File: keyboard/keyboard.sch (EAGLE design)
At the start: 47 parts, among them SW1 CHERRY_MX, SW10 CHERRY_MX, SW11 CHERRY_MX, SW12 CHERRY_MX, SW13 CHERRY_MX, SW14 CHERRY_MX, SW15 CHERRY_MX, SW16 CHERRY_MX, SW17 CHERRY_MX, SW18 CHERRY_MX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

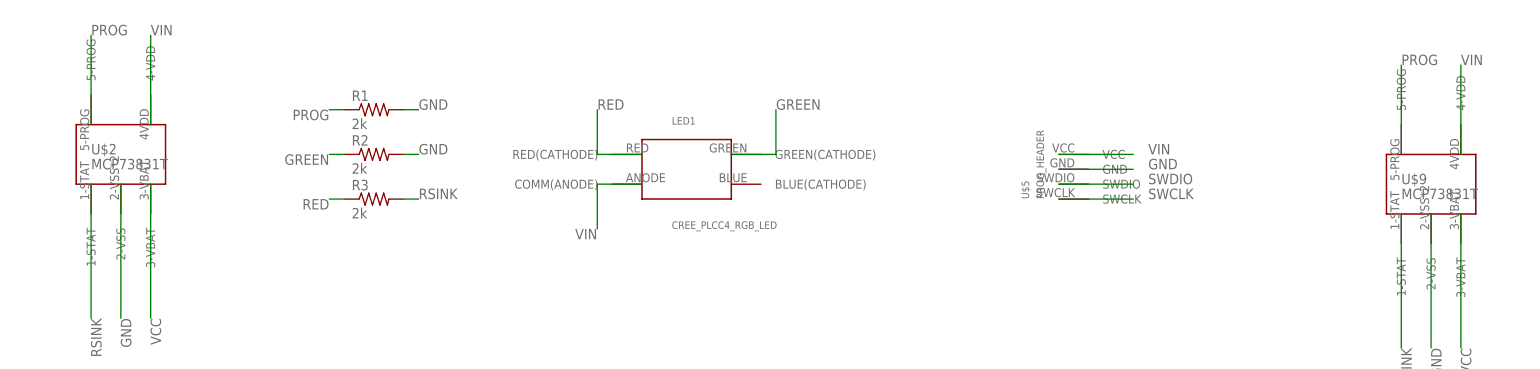
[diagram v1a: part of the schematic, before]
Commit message: redesign heatsink
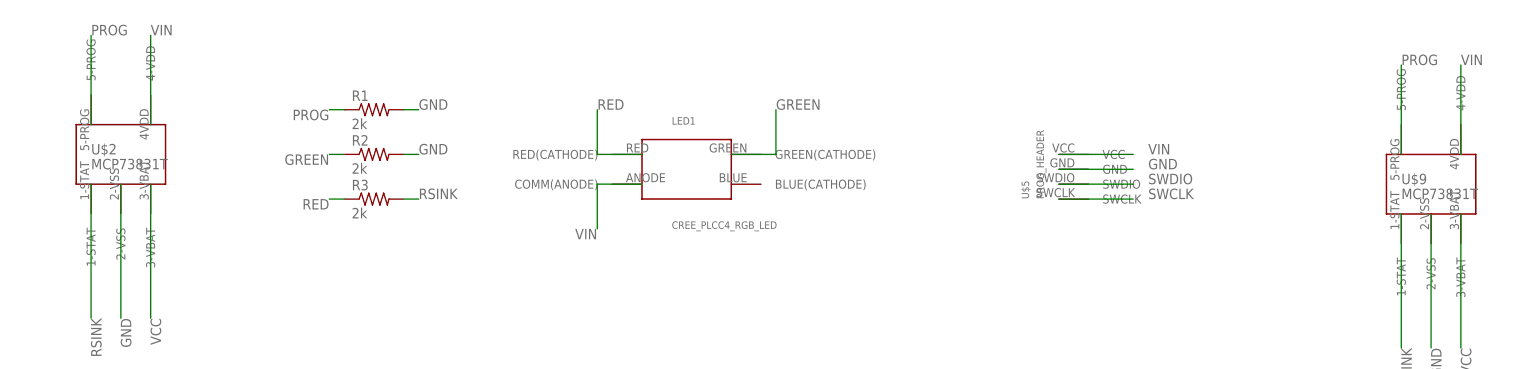
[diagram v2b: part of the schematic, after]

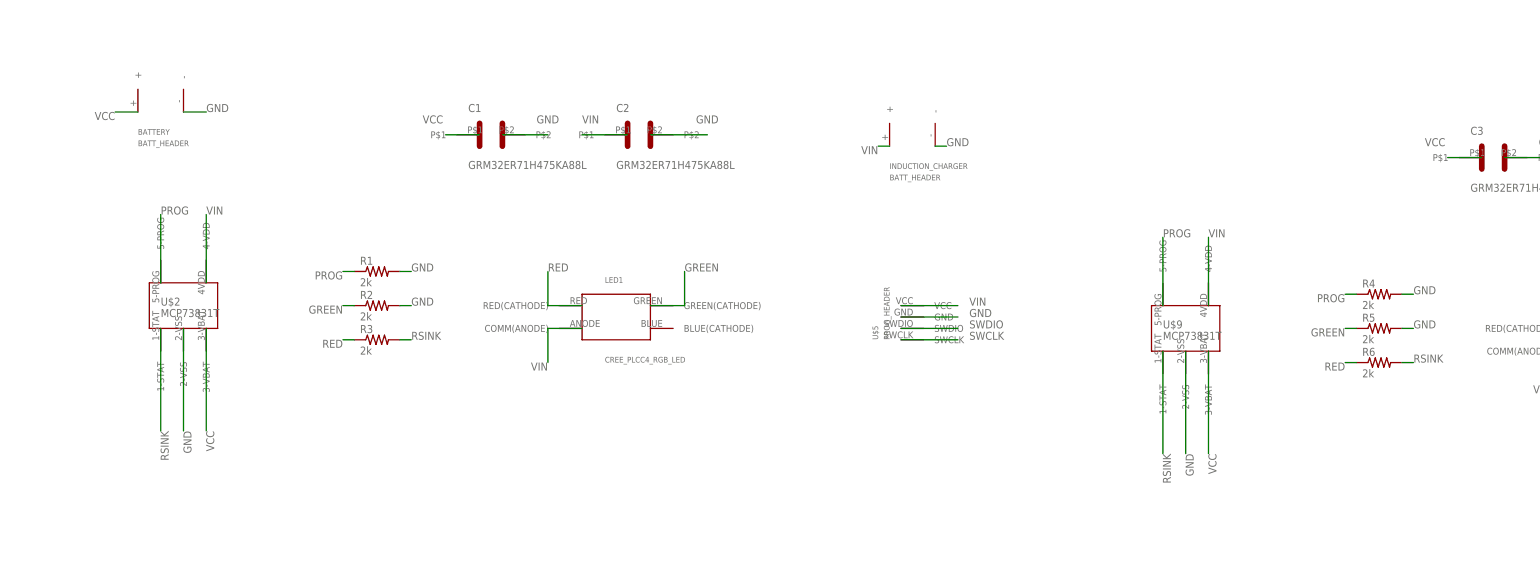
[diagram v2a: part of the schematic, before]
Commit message: add voltage regulator
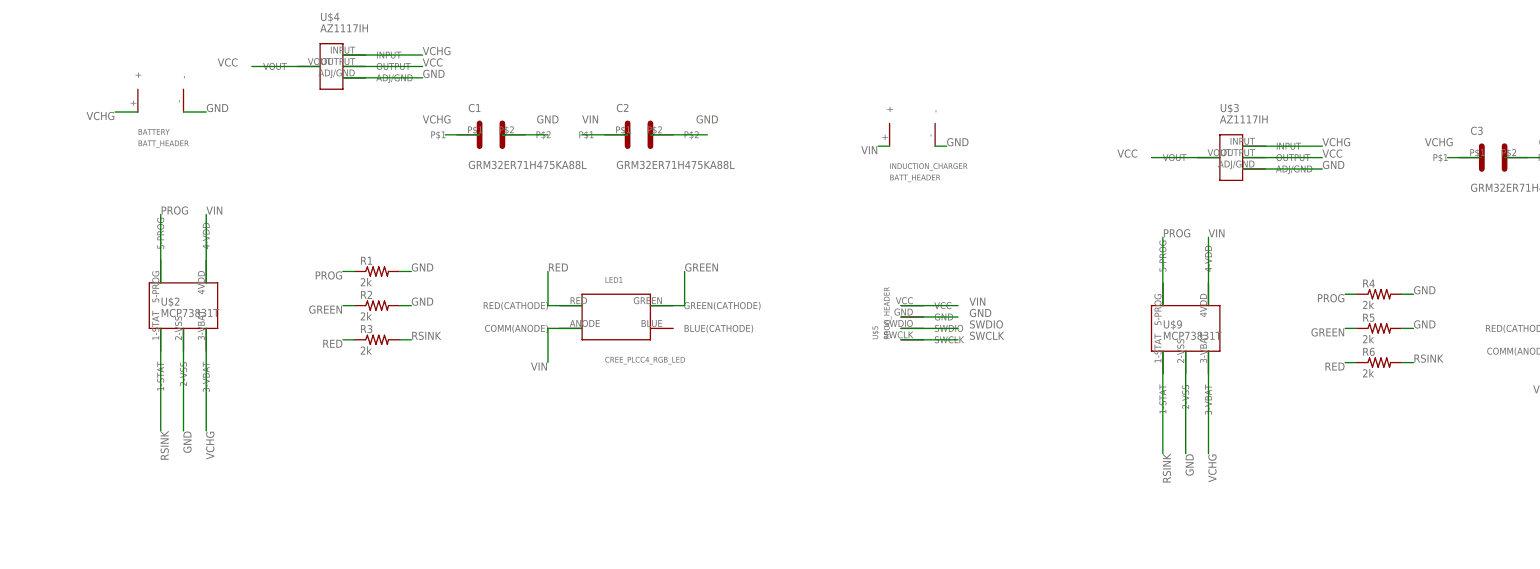
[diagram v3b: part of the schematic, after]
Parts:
- added U$3, U$4: AZ1117IH, az1117ih:AZ1117IH
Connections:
- new net VCHG: BATTERY.+, C1.P$1, C3.P$1, U$2.3-VBAT, U$3.INPUT, U$4.INPUT, U$9.3-VBAT
- net GND: now also U$3.ADJ/GND, U$4.ADJ/GND
- net VCC: now also U$3.OUTPUT, U$3.VOUT, U$4.OUTPUT, U$4.VOUT; no longer BATTERY.+, C1.P$1, C3.P$1, U$2.3-VBAT, U$9.3-VBAT
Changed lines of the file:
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@@
 <?xml version="1.0" encoding="utf-8"?>
 <!DOCTYPE eagle SYSTEM "eagle.dtd">
-<eagle version="8.5.0">
+<eagle version="8.5.2">
 <drawing>
 <settings>
@@
 <part name="INDUCTION_CHARGER" library="batt_header" deviceset="BATT_HEADER" device=""/>
 <part name="BATTERY" library="batt_header" deviceset="BATT_HEADER" device=""/>
+<part name="U$3" library="az1117ih" deviceset="AZ1117IH" device=""/>
+<part name="U$4" library="az1117ih" deviceset="AZ1117IH" device=""/>
 </parts>
 <sheets>
@@
 <instance part="INDUCTION_CHARGER" gate="G$1" x="208.28" y="68.58"/>
 <instance part="BATTERY" gate="G$1" x="40.64" y="76.2"/>
+<instance part="U$3" gate="G$1" x="279.4" y="66.04"/>
+<instance part="U$4" gate="G$1" x="78.74" y="86.36"/>
 </instances>
 <busses>
@@
 <label x="50.8" y="76.2" size="1.778" layer="95"/>
 </segment>
+<segment>
+<pinref part="U$3" gate="G$1" pin="ADJ/GND"/>
+<wire x1="281.94" y1="63.5" x2="299.72" y2="63.5" width="0.1524" layer="91"/>
+<label x="299.72" y="63.5" size="1.778" layer="95"/>
+</segment>
+<segment>
+<pinref part="U$4" gate="G$1" pin="ADJ/GND"/>
+<wire x1="81.28" y1="83.82" x2="99.06" y2="83.82" width="0.1524" layer="91"/>
+<label x="99.06" y="83.82" size="1.778" layer="95"/>
+</segment>
 </net>
 <net name="SW1" class="0">
@@
 </segment>
 <segment>
-<pinref part="U$2" gate="G$1" pin="3-VBAT"/>
-<wire x1="50.8" y1="27.94" x2="50.8" y2="5.08" width="0.1524" layer="91"/>
-<label x="50.8" y="5.08" size="1.778" layer="95" rot="R270"/>
-</segment>
-<segment>
 <pinref part="U$6" gate="G$1" pin="VCC"/>
 <wire x1="236.22" y1="-276.86" x2="218.44" y2="-276.86" width="0.1524" layer="91"/>
@@
 </segment>
 <segment>
-<pinref part="C1" gate="G$1" pin="P$1"/>
-<wire x1="111.76" y1="71.12" x2="104.14" y2="71.12" width="0.1524" layer="91"/>
-<label x="99.06" y="73.66" size="1.778" layer="95"/>
-</segment>
-<segment>
-<pinref part="U$9" gate="G$1" pin="3-VBAT"/>
-<wire x1="274.32" y1="22.86" x2="274.32" y2="0" width="0.1524" layer="91"/>
-<label x="274.32" y="0" size="1.778" layer="95" rot="R270"/>
-</segment>
-<segment>
-<pinref part="C3" gate="G$1" pin="P$1"/>
-<wire x1="335.28" y1="66.04" x2="327.66" y2="66.04" width="0.1524" layer="91"/>
-<label x="322.58" y="68.58" size="1.778" layer="95"/>
-</segment>
-<segment>
-<pinref part="BATTERY" gate="G$1" pin="+"/>
-<wire x1="35.56" y1="76.2" x2="30.48" y2="76.2" width="0.1524" layer="91"/>
-<label x="30.48" y="76.2" size="1.778" layer="95" rot="R180"/>
+<pinref part="U$3" gate="G$1" pin="VOUT"/>
+<wire x1="276.86" y1="66.04" x2="261.62" y2="66.04" width="0.1524" layer="91"/>
+<label x="254" y="66.04" size="1.778" layer="95"/>
+</segment>
+<segment>
+<pinref part="U$3" gate="G$1" pin="OUTPUT"/>
+<wire x1="281.94" y1="66.04" x2="299.72" y2="66.04" width="0.1524" layer="91"/>
+<label x="299.72" y="66.04" size="1.778" layer="95"/>
+</segment>
+<segment>
+<pinref part="U$4" gate="G$1" pin="VOUT"/>
+<wire x1="76.2" y1="86.36" x2="60.96" y2="86.36" width="0.1524" layer="91"/>
+<label x="53.34" y="86.36" size="1.778" layer="95"/>
+</segment>
+<segment>
+<pinref part="U$4" gate="G$1" pin="OUTPUT"/>
+<wire x1="81.28" y1="86.36" x2="99.06" y2="86.36" width="0.1524" layer="91"/>
+<label x="99.06" y="86.36" size="1.778" layer="95"/>
 </segment>
 </net>
@@
 </segment>
 <segment>
+<pinref part="INDUCTION_CHARGER" gate="G$1" pin="+"/>
+<wire x1="203.2" y1="68.58" x2="200.66" y2="68.58" width="0.1524" layer="91"/>
+<label x="200.66" y="68.58" size="1.778" layer="95" rot="R180"/>
+</segment>
+<segment>
 <pinref part="C4" gate="G$1" pin="P$1"/>
 <wire x1="368.3" y1="66.04" x2="358.14" y2="66.04" width="0.1524" layer="91"/>
 <label x="358.14" y="68.58" size="1.778" layer="95"/>
 </segment>
-<segment>
-<pinref part="INDUCTION_CHARGER" gate="G$1" pin="+"/>
-<wire x1="203.2" y1="68.58" x2="200.66" y2="68.58" width="0.1524" layer="91"/>
-<label x="200.66" y="68.58" size="1.778" layer="95" rot="R180"/>
-</segment>
 </net>
 <net name="PROG" class="0">
@@
 </segment>
 </net>
+<net name="VCHG" class="0">
+<segment>
+<pinref part="U$9" gate="G$1" pin="3-VBAT"/>
+<wire x1="274.32" y1="22.86" x2="274.32" y2="0" width="0.1524" layer="91"/>
+<label x="274.32" y="0" size="1.778" layer="95" rot="R270"/>
+</segment>
+<segment>
+<pinref part="U$3" gate="G$1" pin="INPUT"/>
+<wire x1="281.94" y1="68.58" x2="299.72" y2="68.58" width="0.1524" layer="91"/>
+<label x="299.72" y="68.58" size="1.778" layer="95"/>
+</segment>
+<segment>
+<pinref part="U$4" gate="G$1" pin="INPUT"/>
+<wire x1="81.28" y1="88.9" x2="99.06" y2="88.9" width="0.1524" layer="91"/>
+<label x="99.06" y="88.9" size="1.778" layer="95"/>
+</segment>
+<segment>
+<pinref part="BATTERY" gate="G$1" pin="+"/>
+<wire x1="35.56" y1="76.2" x2="30.48" y2="76.2" width="0.1524" layer="91"/>
+<label x="30.48" y="76.2" size="1.778" layer="95" rot="R180"/>
+</segment>
+<segment>
+<pinref part="U$2" gate="G$1" pin="3-VBAT"/>
+<wire x1="50.8" y1="27.94" x2="50.8" y2="5.08" width="0.1524" layer="91"/>
+<label x="50.8" y="5.08" size="1.778" layer="95" rot="R270"/>
+</segment>
+<segment>
+<pinref part="C3" gate="G$1" pin="P$1"/>
+<wire x1="335.28" y1="66.04" x2="327.66" y2="66.04" width="0.1524" layer="91"/>
+<label x="322.58" y="68.58" size="1.778" layer="95"/>
+</segment>
+<segment>
+<pinref part="C1" gate="G$1" pin="P$1"/>
+<wire x1="111.76" y1="71.12" x2="104.14" y2="71.12" width="0.1524" layer="91"/>
+<label x="99.06" y="73.66" size="1.778" layer="95"/>
+</segment>
+</net>
